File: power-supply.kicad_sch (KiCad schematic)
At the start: 38 parts, among them U4 MPM54304GMN, U7 MPM3650GQW-Z

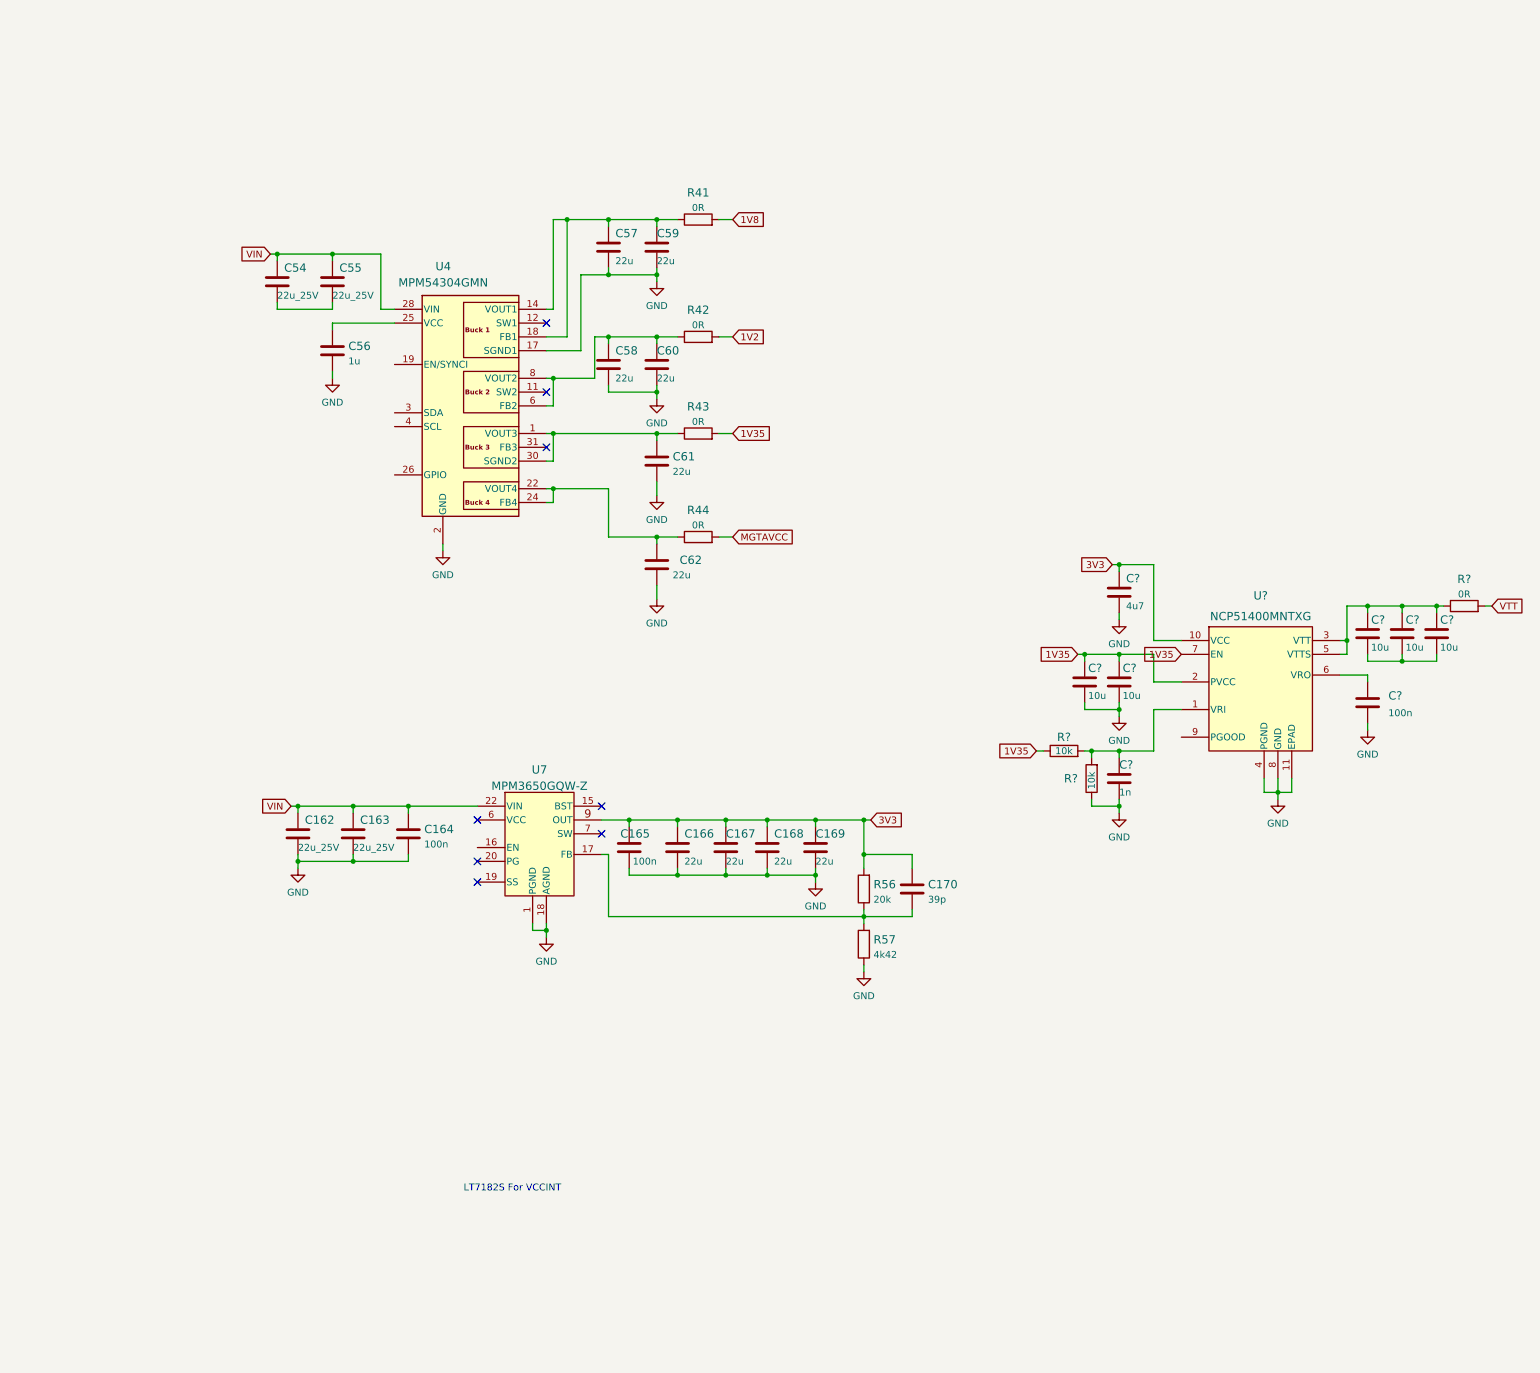
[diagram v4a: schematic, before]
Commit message: Add 1V0 DC-DC, VCCADC and VREFP reference voltages, input jack with reverse polarity protection
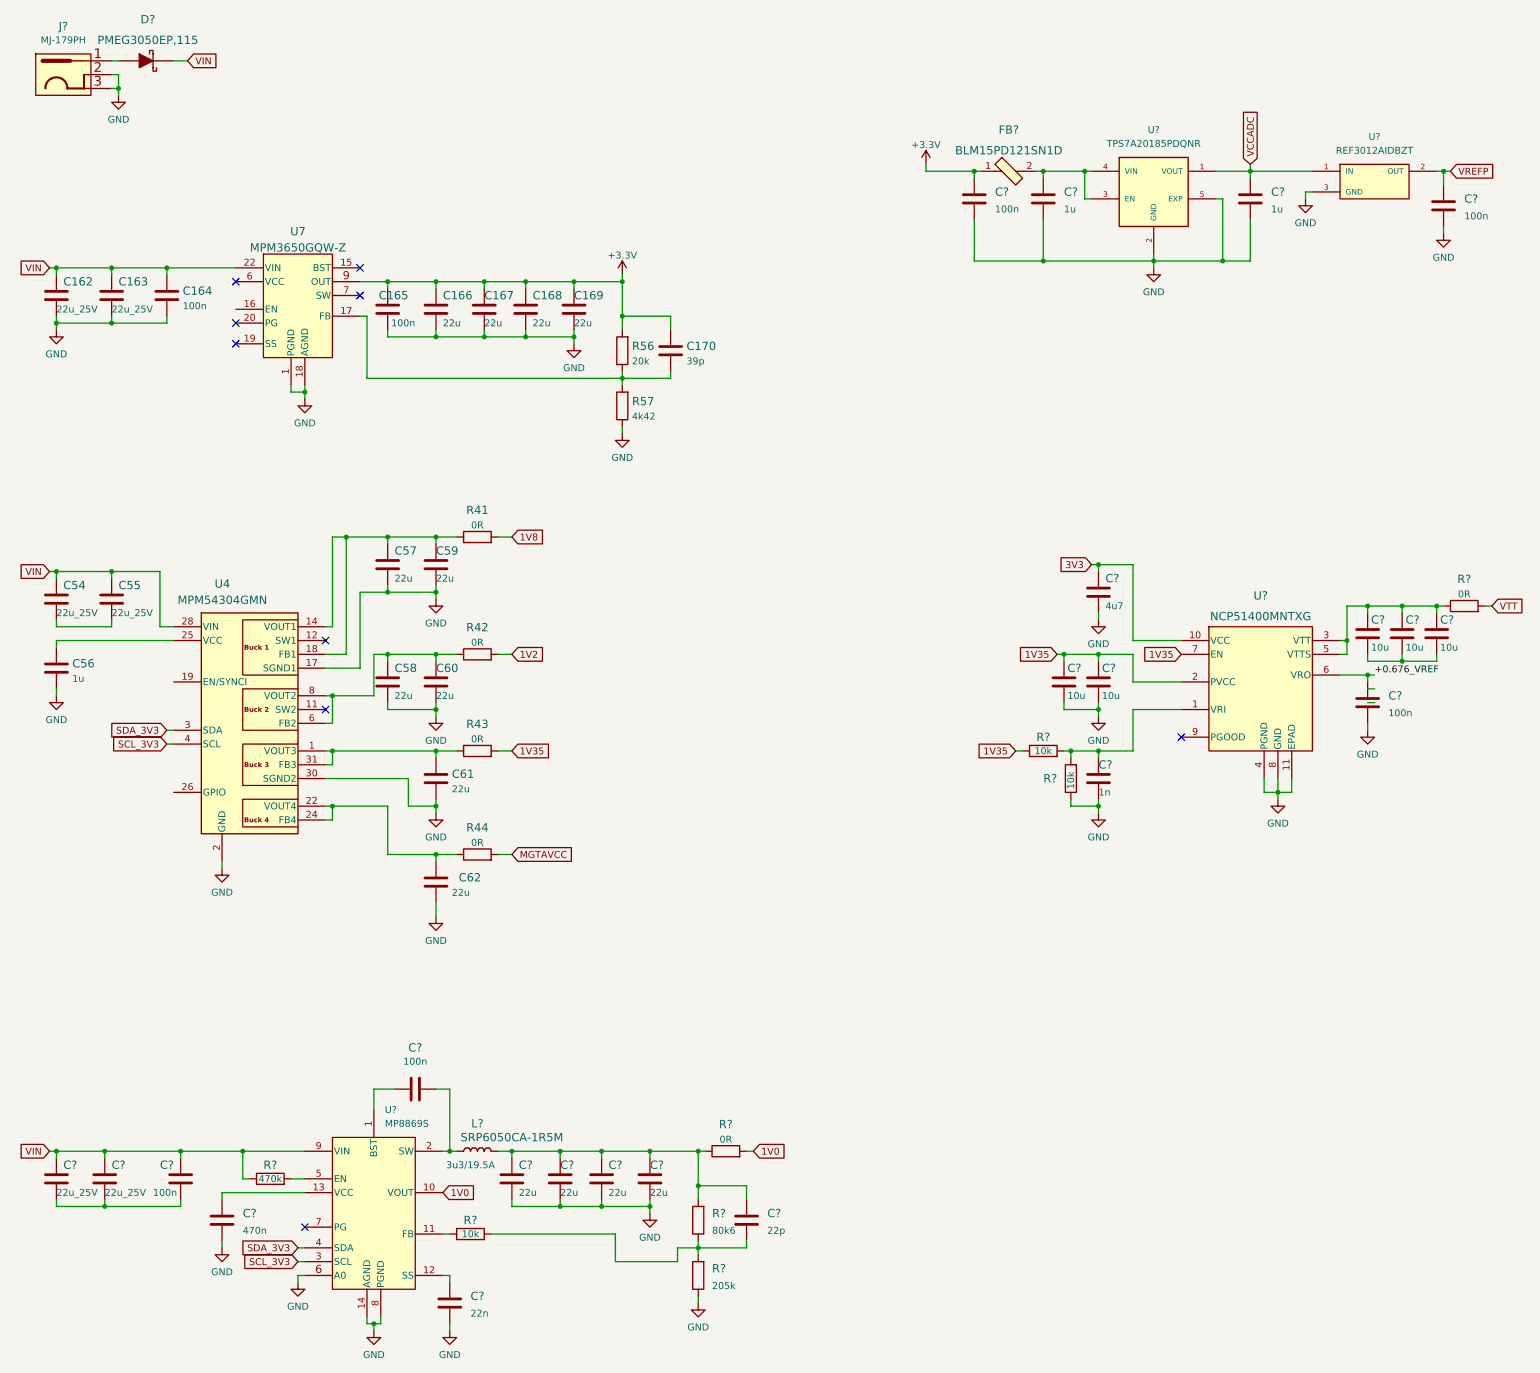
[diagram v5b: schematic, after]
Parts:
- added C? (x2): C_22u_0805_25V, antmicro-footprints:0805-cap, symbol antmicroCapacitorsmisc:C_22u_0805_25V
- added C? (x2): C_1u_0402, antmicro-footprints:0402-cap, symbol antmicroCapacitors0402:C_1u_0402
- added C? (x4): C_100n_0402, antmicro-footprints:0402-cap, symbol antmicroCapacitors0402:C_100n_0402
- added C?: C_22p_0402, antmicro-footprints:0402-cap, symbol antmicroCapacitors0402:C_22p_0402
- added C? (x4): C_22u_0603, antmicro-footprints:0603-cap, symbol antmicroCapacitors0603:C_22u_0603
- added C?: C_22n_0402, antmicro-footprints:0402-cap, symbol antmicroCapacitors0402:C_22n_0402
- added C?: C_470n_0402, antmicro-footprints:0402-cap, symbol antmicroCapacitors0402:C_470n_0402
- added D?: PMEG3050EP,115, antmicro-footprints:Nexperia_SOD128, symbol antmicroDiodesRectifiersSingle:PMEG3050EP,115
- added FB?: BLM15PD121SN1D, antmicro-footprints:0402-res, symbol antmicroFerriteBeadsandChips:BLM15PD121SN1D
- added J?: DC_SOCKET, antmicro-footprints:DC_SOCKET, symbol antmicroBarrelAudioConnectors:DC_SOCKET
- added L?: SRP6050CA-1R5M, antmicro-footprints:Bourns-SRP6050CA, symbol antmicroFixedInductors: SRP6050CA-1R5M
- added R?: R_470k_0402, antmicro-footprints:0402-res, symbol antmicroResistors0402:R_470k_0402
- added R?: R_80k6_0402, antmicro-footprints:0402-res, symbol antmicroResistors0402:R_80k6_0402
- added R?: R_0R_0805, antmicro-footprints:0805-res, symbol antmicroResistorsmisc:R_0R_0805
- added R?: R_10k_0402, antmicro-footprints:0402-res, symbol antmicroResistors0402:R_10k_0402
- added R?: R_205k_0402, antmicro-footprints:0402-res, symbol antmicroResistors0402:R_205k_0402
- added U?: REF3012AIDBZT, antmicro-footprints:SOT-23-3, symbol antmicroPMICPowerDistributionSwitchesLoadDrivers:REF3012AIDBZT
- added U?: TPS7A20185PDQNR, antmicro-footprints:XDFN4, symbol antmicroPMICVoltageRegulatorsLinear:TPS7A20185PDQNR
- added U?: MP8869S, antmicro-footprints:MPS_QFN-14_MP8869S, symbol antmicroPMICVoltageRegulatorsDCDCSwitchingRegulators:MP8869S
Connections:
- net 3V3: no longer C165.1, C166.1, C167.1, C168.1, C169.1, C170.1, R56.2, U7.10 (OUT), U7.11 (OUT), U7.12 (OUT), U7.9 (OUT)
- net GND: now also U4.30 (SGND2), C?.2, C?.2, C?.2, C?.2, C?.2, C?.2, C?.2, C?.2, C?.2, C?.2, J?.2, J?.3, R?.1, U?.14 (AGND), U?.2 (GND), U?.3 (GND), U?.5 (EXP), U?.6 (A0), U?.8 (PGND)
- net VIN: now also C?.1, C?.1, C?.1, D?.1, R?.1, U?.9 (VIN)
- net +0.676_VREF: now reaches C?.1, U?.6 (VRO)
- net at C61.1, R43.1, U4.1 (VOUT3)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: now also U4.31 (FB3); no longer U4.30 (SGND2)
- net SDA_3V3: now reaches U4.3 (SDA)
- net SDA_3V3: now also U?.4 (SDA)
- net SCL_3V3: now reaches U4.4 (SCL)
- net SCL_3V3: now also U?.3 (SCL)
- new net: C?.2, C?.2, C?.2
- new net: C?.1, FB?.2, U?.3 (EN), U?.4 (VIN)
- new net: D?.2, J?.1
- new net: R?.2, U?.5 (EN)
- new net: C?.1, U?.1 (BST)
- new net: C?.2, L?.1 (P), U?.2 (SW)
- new net: C?.1, C?.1, C?.1, C?.1, C?.1, L?.2 (P), R?.1, R?.2
- new net: C?.2, R?.1, R?.2, R?.2
- new net: C?.1, U?.12 (SS)
- new net: R?.1, U?.11 (FB)
- new net: C?.1, U?.13 (VCC)
- new net +3V3: C165.1, C166.1, C167.1, C168.1, C169.1, C170.1, C?.1, FB?.1, R56.2, U7.10 (OUT), U7.11 (OUT), U7.12 (OUT), U7.9 (OUT)
- new net 1V0: R?.2, U?.10 (VOUT)
- new net VCCADC: C?.1, U?.1 (IN), U?.1 (VOUT)
- new net VREFP: C?.1, U?.2 (OUT)
- no-connect marks 8 -> 9
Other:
- note removed: "LT7182S For VCCINT"
- moved on the sheet: C162, C163, C164, C165, C166, C167, C168, C169, C170, C54, C55, C56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

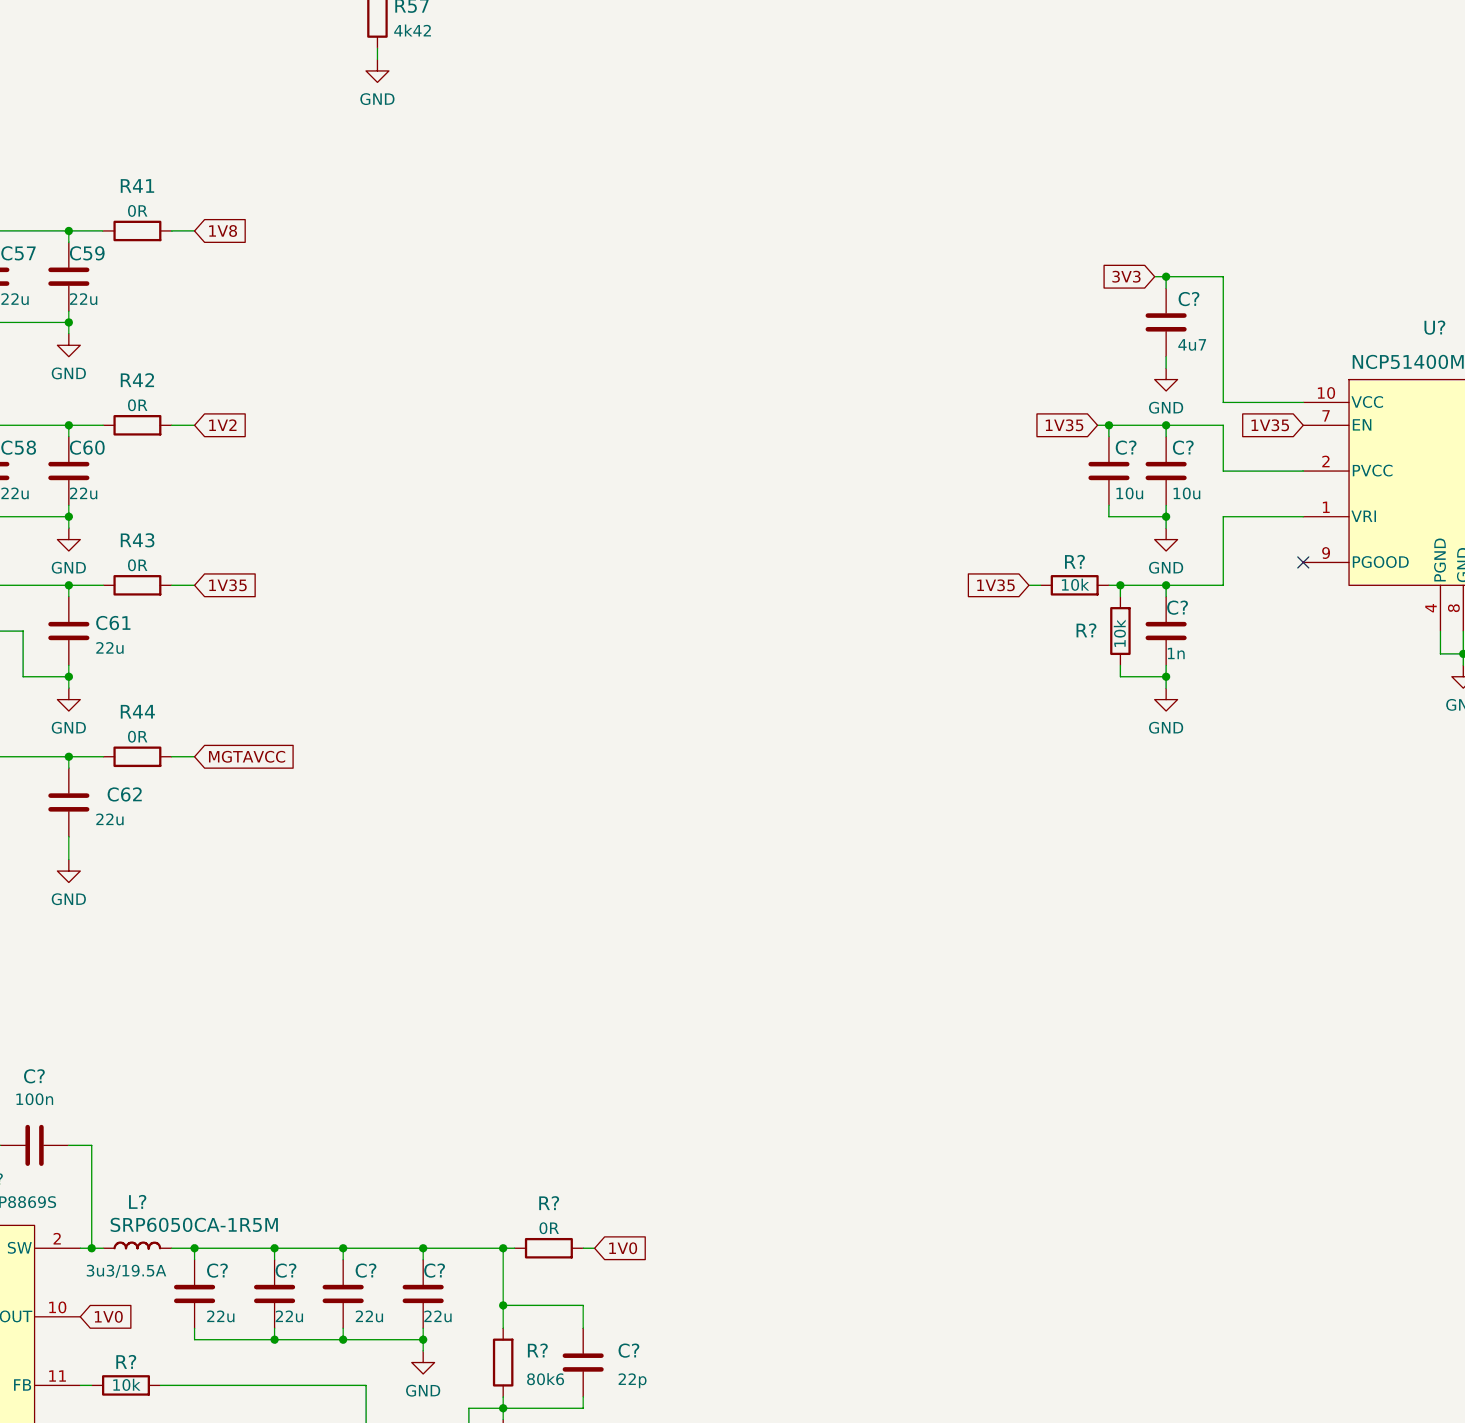
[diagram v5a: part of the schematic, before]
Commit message: Replace labels with power symbols
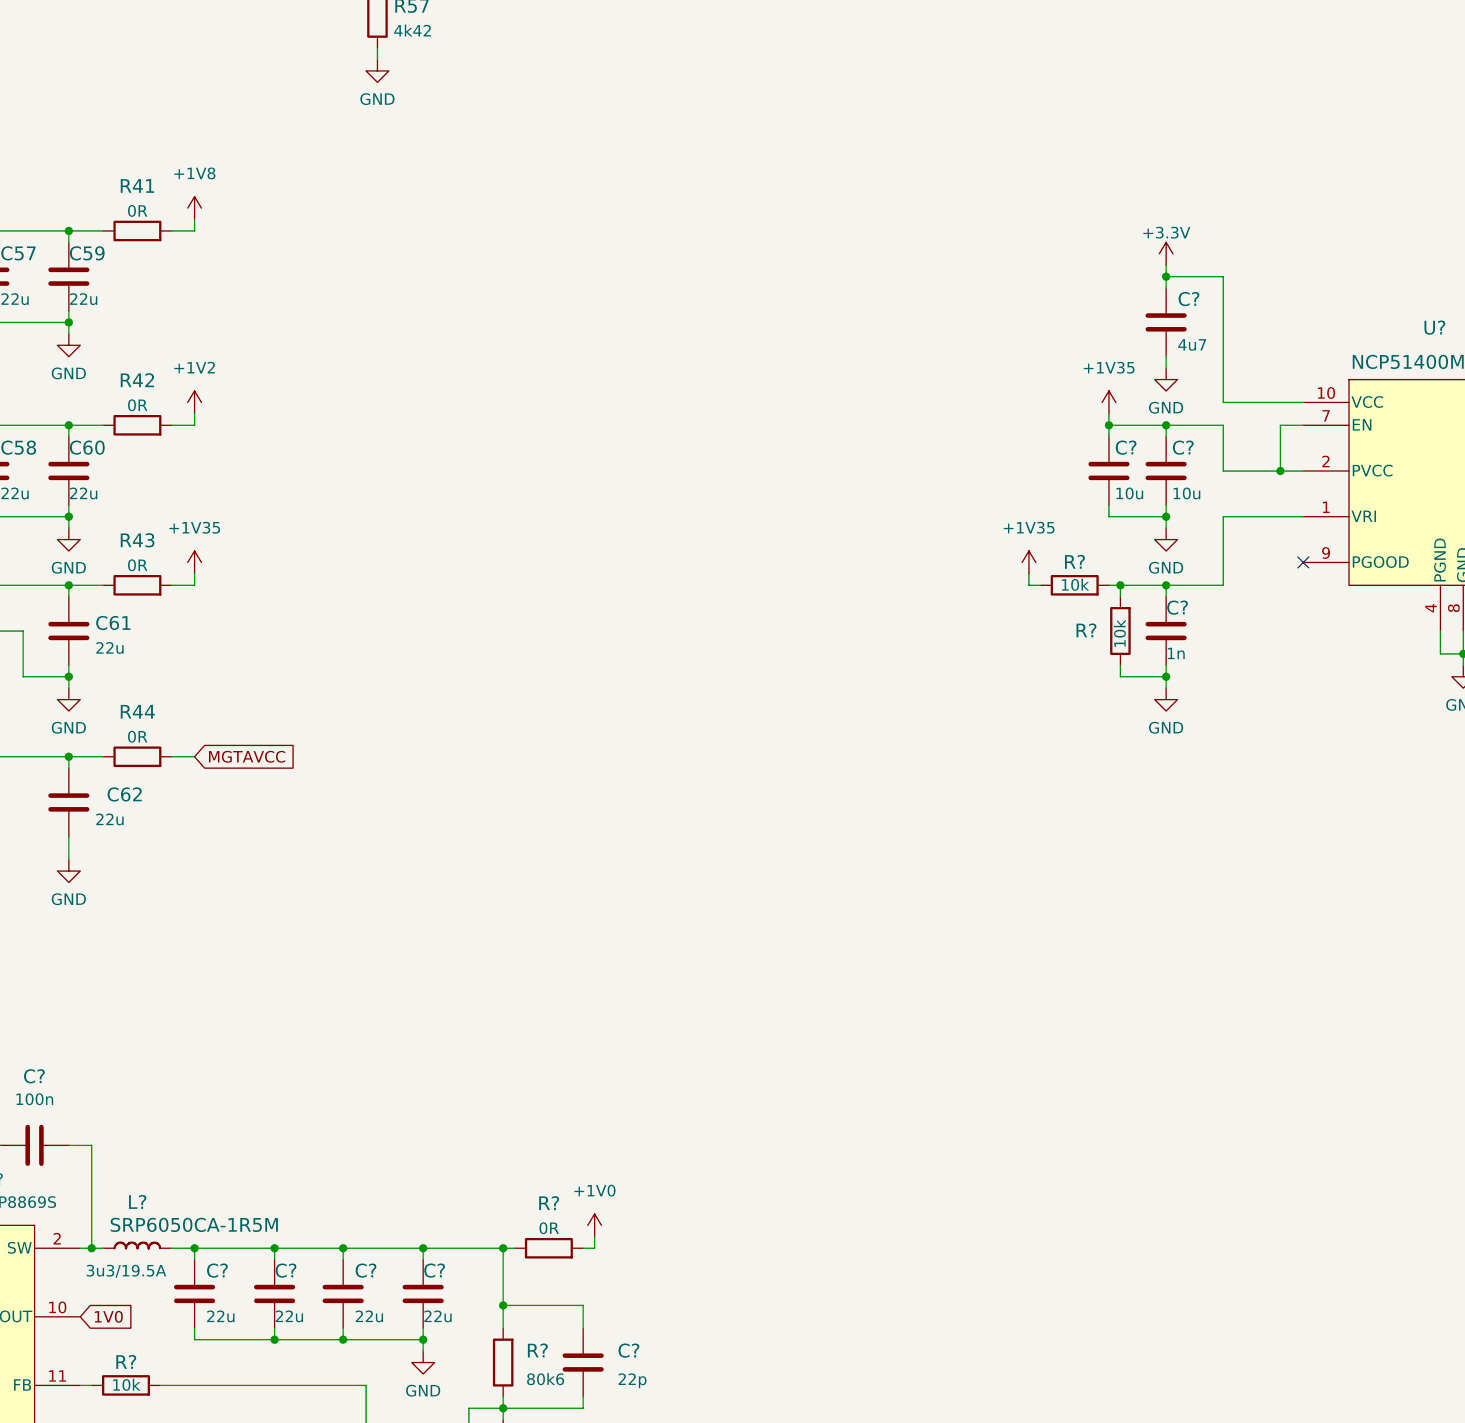
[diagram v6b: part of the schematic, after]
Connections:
- net 3V3 is gone; now on net +3V3: C?.1, U?.10 (VCC)
- net 1V0: no longer R?.2
- net 1V2 renamed +1V2
- net 1V35 renamed +1V35
- net 1V8 renamed +1V8
- new net +1V0: R?.2
